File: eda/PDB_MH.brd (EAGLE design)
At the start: 101.6 x 81.3 mm, 18 parts

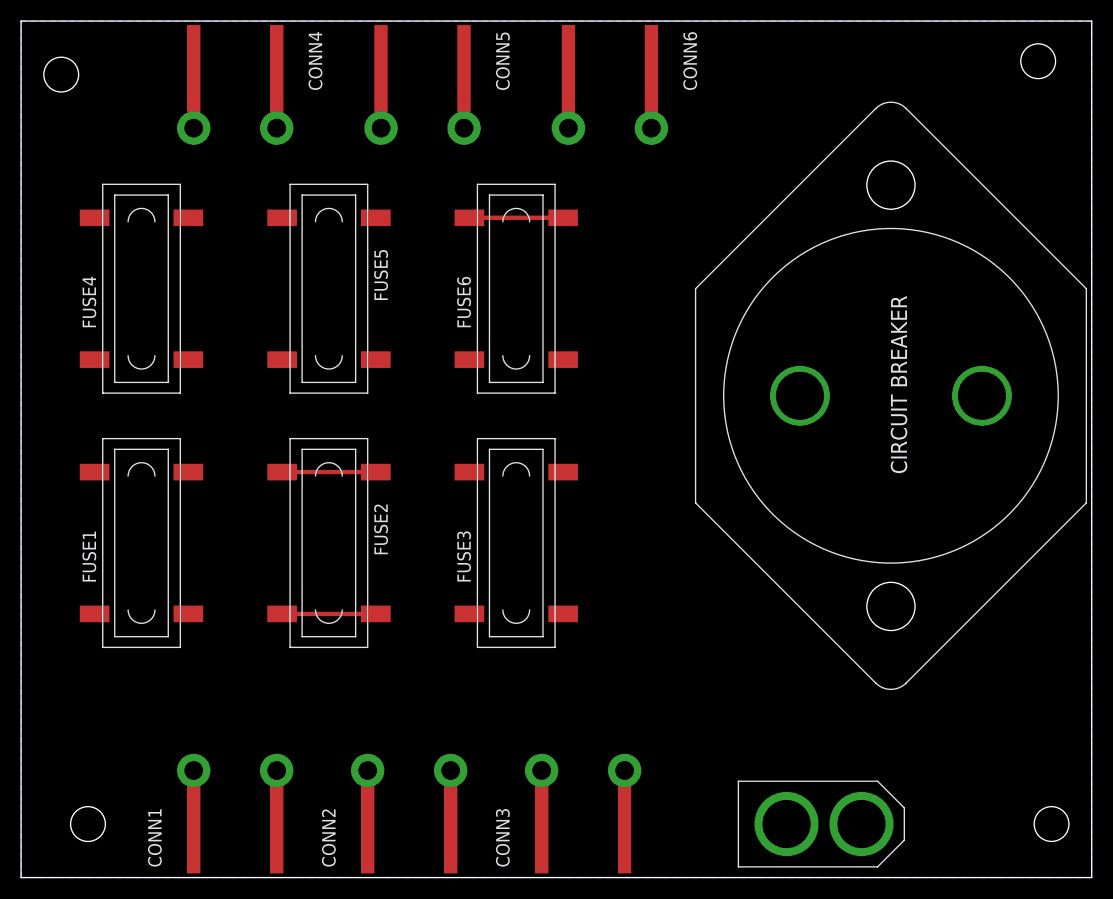
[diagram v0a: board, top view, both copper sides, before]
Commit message: Completed PDB board: have added the power planes for all connectors
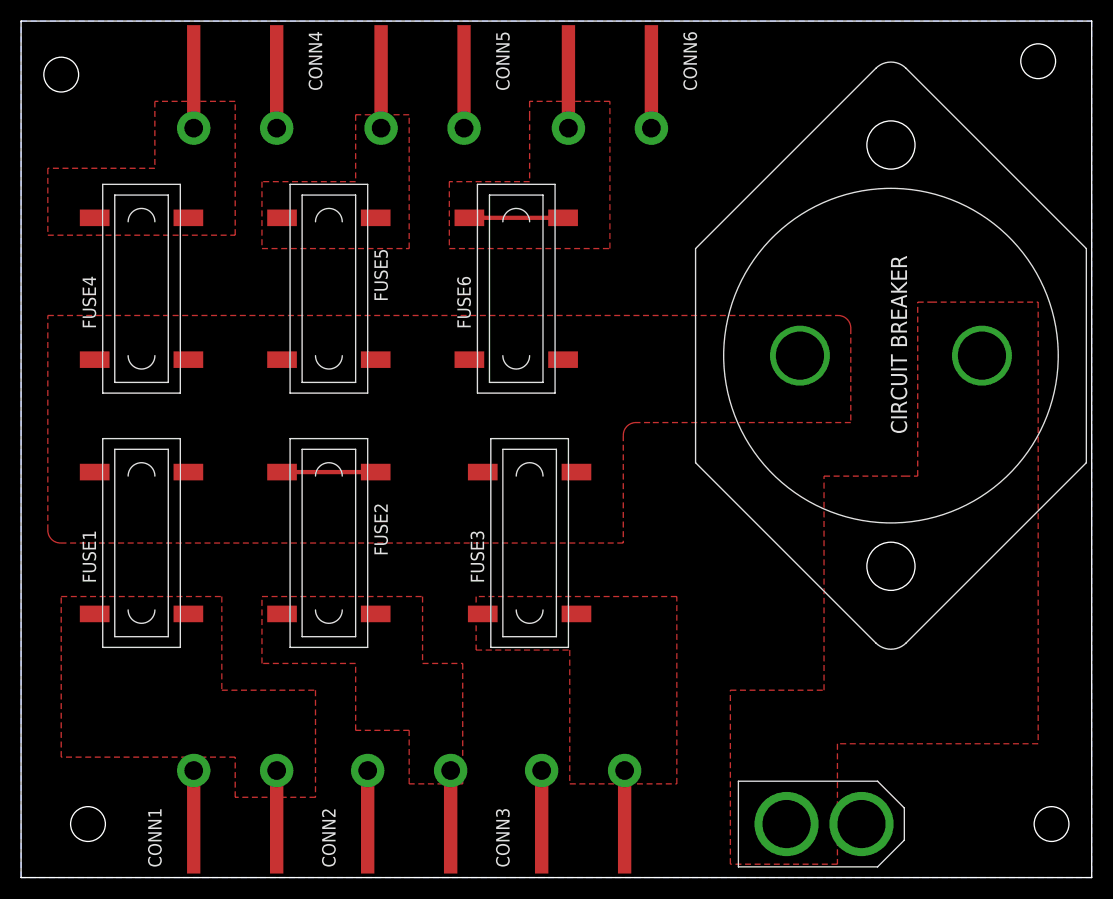
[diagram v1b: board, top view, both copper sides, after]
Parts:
- moved CIRCUIT_BREAKER 3.81 mm to (82.5, 49.5)
- moved FUSE3 1.27 mm to (48.3, 31.8)
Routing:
- net VOUT2: track 14.2 -> 5.33 mm
- added copper zone on layer 1, net 12V
- added copper zone on layer 1, net BAT
- added copper zone on layer 1, net VOUT1
- added copper zone on layer 1, net VOUT2
- added copper zone on layer 1, net VOUT3
- added copper zone on layer 1, net VOUT4
- added copper zone on layer 1, net VOUT5
- added copper zone on layer 1, net VOUT6
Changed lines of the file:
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@@
 <attribute name="PARTNUMBER" value="PRT-10474 " x="76.2" y="5.08" size="1.778" layer="27" display="off"/>
 </element>
-<element name="CIRCUIT_BREAKER" library="pie" package="CIRC_BREAKER" value="CIRC_BREAKER" x="82.55" y="45.72" rot="R270">
-<attribute name="MANUF" value="WAYTEK" x="82.55" y="45.72" size="1.778" layer="27" rot="R270" display="off"/>
-<attribute name="MANUF-PN" value="46977" x="82.55" y="45.72" size="1.778" layer="27" rot="R270" display="off"/>
+<element name="CIRCUIT_BREAKER" library="pie" package="CIRC_BREAKER" value="CIRC_BREAKER" x="82.55" y="49.53" rot="R270">
+<attribute name="MANUF" value="WAYTEK" x="82.55" y="49.53" size="1.778" layer="27" rot="R270" display="off"/>
+<attribute name="MANUF-PN" value="46977" x="82.55" y="49.53" size="1.778" layer="27" rot="R270" display="off"/>
 </element>
 <element name="FUSE2" library="pie" package="FUSE_HOLDER_SMD" value="FUSE_HOLDER_SMD" x="29.21" y="31.75" rot="R270">
@@
 <attribute name="MANUF-PN" value="3587" x="11.43" y="31.75" size="1.778" layer="27" rot="R90" display="off"/>
 </element>
-<element name="FUSE3" library="pie" package="FUSE_HOLDER_SMD" value="FUSE_HOLDER_SMD" x="46.99" y="31.75" rot="R90">
-<attribute name="DIGIKEY-PN" value=" 36-3587-ND" x="46.99" y="31.75" size="1.778" layer="27" rot="R90" display="off"/>
-<attribute name="MANUF" value="KEYSTONE" x="46.99" y="31.75" size="1.778" layer="27" rot="R90" display="off"/>
-<attribute name="MANUF-PN" value="3587" x="46.99" y="31.75" size="1.778" layer="27" rot="R90" display="off"/>
+<element name="FUSE3" library="pie" package="FUSE_HOLDER_SMD" value="FUSE_HOLDER_SMD" x="48.26" y="31.75" rot="R90">
+<attribute name="DIGIKEY-PN" value=" 36-3587-ND" x="48.26" y="31.75" size="1.778" layer="27" rot="R90" display="off"/>
+<attribute name="MANUF" value="KEYSTONE" x="48.26" y="31.75" size="1.778" layer="27" rot="R90" display="off"/>
+<attribute name="MANUF-PN" value="3587" x="48.26" y="31.75" size="1.778" layer="27" rot="R90" display="off"/>
 </element>
 <element name="FUSE4" library="pie" package="FUSE_HOLDER_SMD" value="FUSE_HOLDER_SMD" x="11.43" y="55.88" rot="R90">
@@
 <signals>
 <signal name="GND">
-<polygon width="0.4064" layer="16">
+<polygon width="1.1938" layer="16">
 <vertex x="0" y="81.28"/>
 <vertex x="101.6" y="81.28"/>
@@
 <contactref element="FUSE6" pad="P$1_DOWN"/>
 <wire x1="33.655" y1="38.481" x2="24.765" y2="38.481" width="0.4064" layer="1"/>
-<wire x1="51.435" y1="49.149" x2="73.914" y2="45.72" width="0" layer="19" extent="1-1"/>
-<wire x1="42.545" y1="49.149" x2="51.435" y2="49.149" width="0" layer="19" extent="1-1"/>
-<wire x1="33.655" y1="49.149" x2="42.545" y2="49.149" width="0" layer="19" extent="1-1"/>
-<wire x1="24.765" y1="49.149" x2="33.655" y2="49.149" width="0" layer="19" extent="1-1"/>
-<wire x1="15.875" y1="49.149" x2="24.765" y2="49.149" width="0" layer="19" extent="1-1"/>
-<wire x1="6.985" y1="49.149" x2="15.875" y2="49.149" width="0" layer="19" extent="1-1"/>
-<wire x1="51.435" y1="38.481" x2="51.435" y2="49.149" width="0" layer="19" extent="1-1"/>
-<wire x1="42.545" y1="38.481" x2="51.435" y2="38.481" width="0" layer="19" extent="1-1"/>
-<wire x1="33.655" y1="38.481" x2="42.545" y2="38.481" width="0" layer="19" extent="1-1"/>
-<wire x1="15.875" y1="38.481" x2="24.765" y2="38.481" width="0" layer="19" extent="1-1"/>
-<wire x1="6.985" y1="38.481" x2="15.875" y2="38.481" width="0" layer="19" extent="1-1"/>
+<polygon width="1.1938" layer="1">
+<vertex x="2.54" y="53.34"/>
+<vertex x="77.5462" y="53.34" curve="-90"/>
+<vertex x="78.74" y="52.1462"/>
+<vertex x="78.74" y="43.18"/>
+<vertex x="59.69" y="43.18"/>
+<vertex x="58.3438" y="43.18" curve="90"/>
+<vertex x="57.15" y="41.9862"/>
+<vertex x="57.15" y="31.75"/>
+<vertex x="3.7338" y="31.75" curve="-90"/>
+<vertex x="2.54" y="32.9438"/>
+</polygon>
 </signal>
 <signal name="VOUT1">
@@
 <contactref element="FUSE1" pad="P$1_DOWN"/>
 <wire x1="24.257" y1="10.16" x2="24.257" y2="4.826" width="0.4064" layer="1"/>
-<wire x1="6.985" y1="25.019" x2="15.875" y2="25.019" width="0" layer="19" extent="1-1"/>
-<wire x1="24.257" y1="10.16" x2="15.875" y2="25.019" width="0" layer="19" extent="1-1"/>
+<polygon width="1.1938" layer="1">
+<vertex x="3.81" y="26.67"/>
+<vertex x="19.05" y="26.67"/>
+<vertex x="19.05" y="17.78"/>
+<vertex x="27.94" y="17.78"/>
+<vertex x="27.94" y="7.62"/>
+<vertex x="20.32" y="7.62"/>
+<vertex x="20.32" y="11.43"/>
+<vertex x="3.81" y="11.43"/>
+</polygon>
 </signal>
 <signal name="VOUT3">
@@
 <contactref element="FUSE3" pad="P$1_DOWN"/>
 <wire x1="57.277" y1="10.16" x2="57.277" y2="4.826" width="0.4064" layer="1"/>
-<wire x1="42.545" y1="25.019" x2="51.435" y2="25.019" width="0" layer="19" extent="1-1"/>
-<wire x1="57.277" y1="10.16" x2="51.435" y2="25.019" width="0" layer="19" extent="1-1"/>
+<polygon width="1.1938" layer="1">
+<vertex x="43.18" y="26.67"/>
+<vertex x="43.18" y="21.59"/>
+<vertex x="52.07" y="21.59"/>
+<vertex x="52.07" y="8.89"/>
+<vertex x="62.23" y="8.89"/>
+<vertex x="62.23" y="26.67"/>
+</polygon>
 </signal>
 <signal name="VOUT2">
@@
 <contactref element="FUSE2" pad="P$2_DOWN"/>
 <wire x1="40.767" y1="10.16" x2="40.767" y2="4.826" width="0.4064" layer="1"/>
-<wire x1="24.765" y1="25.019" x2="33.655" y2="25.019" width="0.4064" layer="1"/>
-<wire x1="40.767" y1="10.16" x2="33.655" y2="25.019" width="0" layer="19" extent="1-1"/>
+<polygon width="1.1938" layer="1">
+<vertex x="22.86" y="26.67"/>
+<vertex x="38.1" y="26.67"/>
+<vertex x="38.1" y="20.32"/>
+<vertex x="41.91" y="20.32"/>
+<vertex x="41.91" y="8.89"/>
+<vertex x="36.83" y="8.89"/>
+<vertex x="36.83" y="13.97"/>
+<vertex x="31.75" y="13.97"/>
+<vertex x="31.75" y="20.32"/>
+<vertex x="22.86" y="20.32"/>
+</polygon>
 </signal>
 <signal name="VOUT4">
@@
 <contactref element="CONN4" pad="PIN2-LEAD"/>
 <wire x1="16.383" y1="71.12" x2="16.383" y2="76.454" width="0.4064" layer="1"/>
-<wire x1="15.875" y1="62.611" x2="16.383" y2="71.12" width="0" layer="19" extent="1-1"/>
-<wire x1="6.985" y1="62.611" x2="15.875" y2="62.611" width="0" layer="19" extent="1-1"/>
+<polygon width="1.1938" layer="1">
+<vertex x="2.54" y="60.96"/>
+<vertex x="20.32" y="60.96"/>
+<vertex x="20.32" y="73.66"/>
+<vertex x="12.7" y="73.66"/>
+<vertex x="12.7" y="67.31"/>
+<vertex x="2.54" y="67.31"/>
+</polygon>
 </signal>
 <signal name="VOUT5">
@@
 <contactref element="CONN5" pad="PIN2-LEAD"/>
 <wire x1="34.163" y1="71.12" x2="34.163" y2="76.454" width="0.4064" layer="1"/>
-<wire x1="33.655" y1="62.611" x2="34.163" y2="71.12" width="0" layer="19" extent="1-1"/>
-<wire x1="24.765" y1="62.611" x2="33.655" y2="62.611" width="0" layer="19" extent="1-1"/>
+<polygon width="1.1938" layer="1">
+<vertex x="31.75" y="72.39"/>
+<vertex x="31.75" y="66.04"/>
+<vertex x="22.86" y="66.04"/>
+<vertex x="22.86" y="59.69"/>
+<vertex x="36.83" y="59.69"/>
+<vertex x="36.83" y="72.39"/>
+</polygon>
 </signal>
 <signal name="BAT">
 <contactref element="CIRCUIT_BREAKER" pad="P$1"/>
 <contactref element="U$1" pad="12V"/>
-<wire x1="72.644" y1="5.08" x2="91.186" y2="45.72" width="0" layer="19" extent="1-1"/>
+<polygon width="1.1938" layer="1">
+<vertex x="86.36" y="54.61"/>
+<vertex x="96.52" y="54.61"/>
+<vertex x="96.52" y="12.7"/>
+<vertex x="77.47" y="12.7"/>
+<vertex x="77.47" y="1.27"/>
+<vertex x="67.31" y="1.27"/>
+<vertex x="67.31" y="17.78"/>
+<vertex x="76.2" y="17.78"/>
+<vertex x="76.2" y="38.1"/>
+<vertex x="83.82" y="38.1"/>
+<vertex x="85.09" y="38.1"/>
+<vertex x="85.09" y="54.61"/>
+</polygon>
 </signal>
 <signal name="VOUT6">
@@
 <wire x1="51.943" y1="71.12" x2="51.943" y2="76.454" width="0.4064" layer="1"/>
 <wire x1="42.545" y1="62.611" x2="51.435" y2="62.611" width="0.4064" layer="1"/>
-<wire x1="51.435" y1="62.611" x2="51.943" y2="71.12" width="0" layer="19" extent="1-1"/>
+<polygon width="1.1938" layer="1">
+<vertex x="48.26" y="72.39"/>
+<vertex x="48.26" y="66.04"/>
+<vertex x="40.64" y="66.04"/>
+<vertex x="40.64" y="59.69"/>
+<vertex x="55.88" y="59.69"/>
+<vertex x="55.88" y="73.66"/>
+<vertex x="48.26" y="73.66"/>
+</polygon>
 </signal>
 </signals>

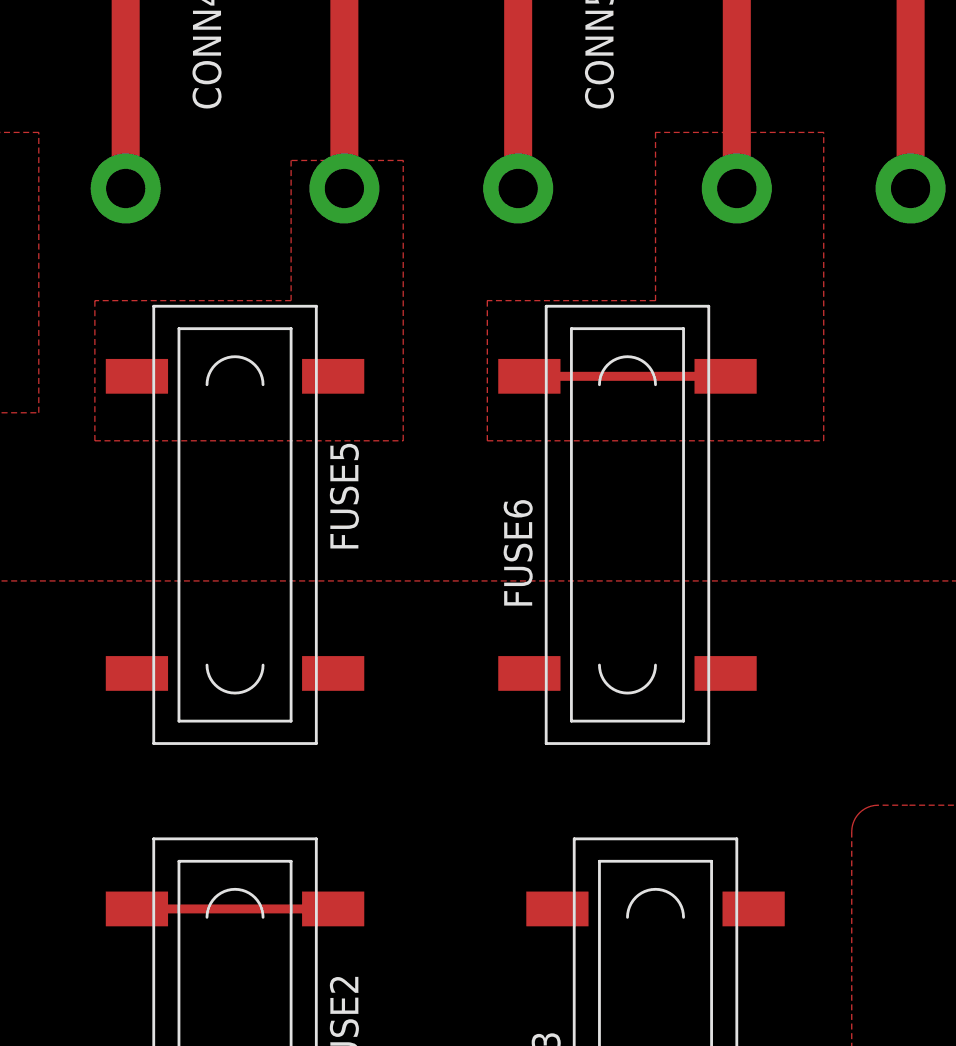
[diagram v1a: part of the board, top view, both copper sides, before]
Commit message: Corrected the polygons within the routes
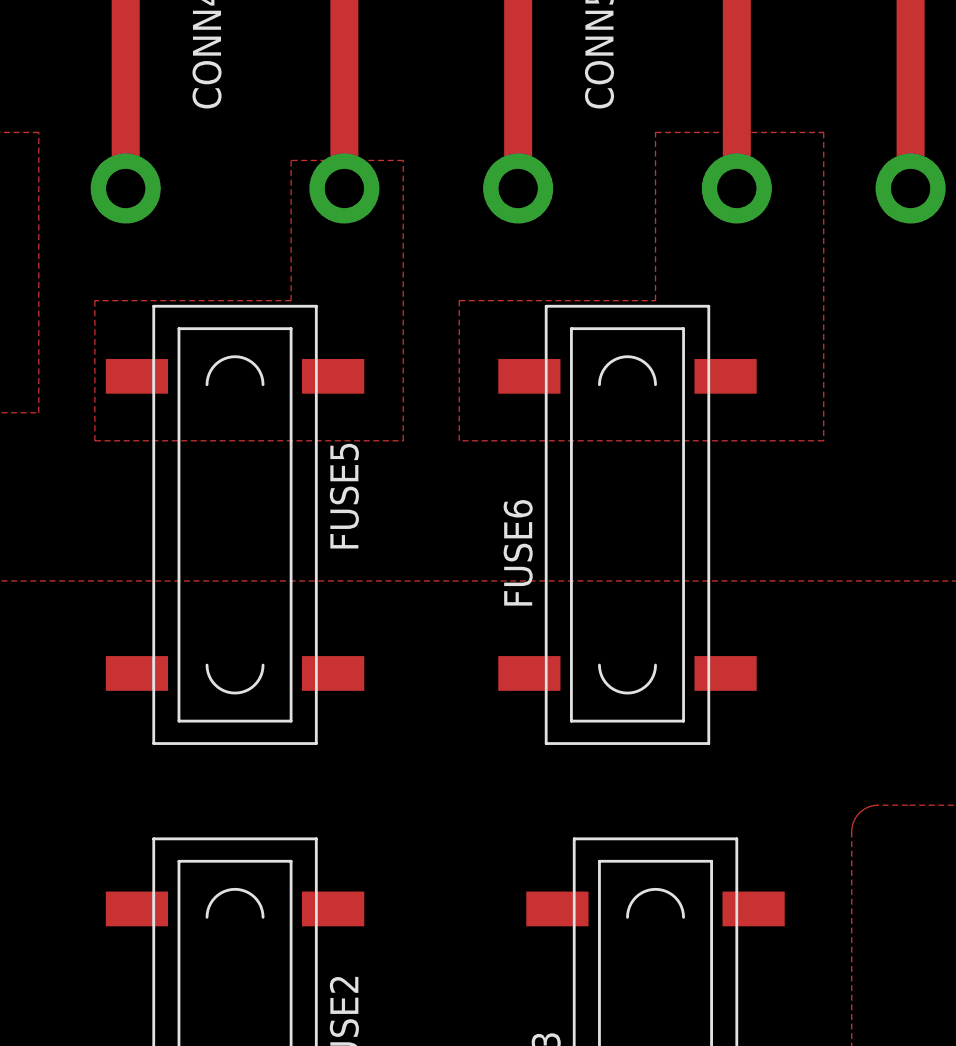
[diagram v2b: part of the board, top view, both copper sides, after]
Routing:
- net VOUT6: track 14.2 -> 5.33 mm
- net 12V: track 8.89 -> 0.00 mm
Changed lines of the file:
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@@
 <contactref element="FUSE6" pad="P$1_UP"/>
 <contactref element="FUSE6" pad="P$1_DOWN"/>
-<wire x1="33.655" y1="38.481" x2="24.765" y2="38.481" width="0.4064" layer="1"/>
 <polygon width="1.1938" layer="1">
 <vertex x="2.54" y="53.34"/>
@@
 <contactref element="CONN6" pad="PIN2-LEAD"/>
 <wire x1="51.943" y1="71.12" x2="51.943" y2="76.454" width="0.4064" layer="1"/>
-<wire x1="42.545" y1="62.611" x2="51.435" y2="62.611" width="0.4064" layer="1"/>
 <polygon width="1.1938" layer="1">
-<vertex x="48.26" y="72.39"/>
+<vertex x="48.26" y="73.66"/>
+<vertex x="55.88" y="73.66"/>
+<vertex x="55.88" y="59.69"/>
+<vertex x="39.37" y="59.69"/>
+<vertex x="39.37" y="66.04"/>
 <vertex x="48.26" y="66.04"/>
-<vertex x="40.64" y="66.04"/>
-<vertex x="40.64" y="59.69"/>
-<vertex x="55.88" y="59.69"/>
-<vertex x="55.88" y="73.66"/>
-<vertex x="48.26" y="73.66"/>
 </polygon>
 </signal>
